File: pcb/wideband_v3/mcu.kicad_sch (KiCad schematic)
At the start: 44 parts, among them J1 Conn_01x14, J2 USB_C_Receptacle_USB2.0, J3 Tag connect, SW1 Key0, SW3 Key1, U1 RP2040, U2 W25Q128JVS, U8 AMS1117-3.3, Y1 12MHz

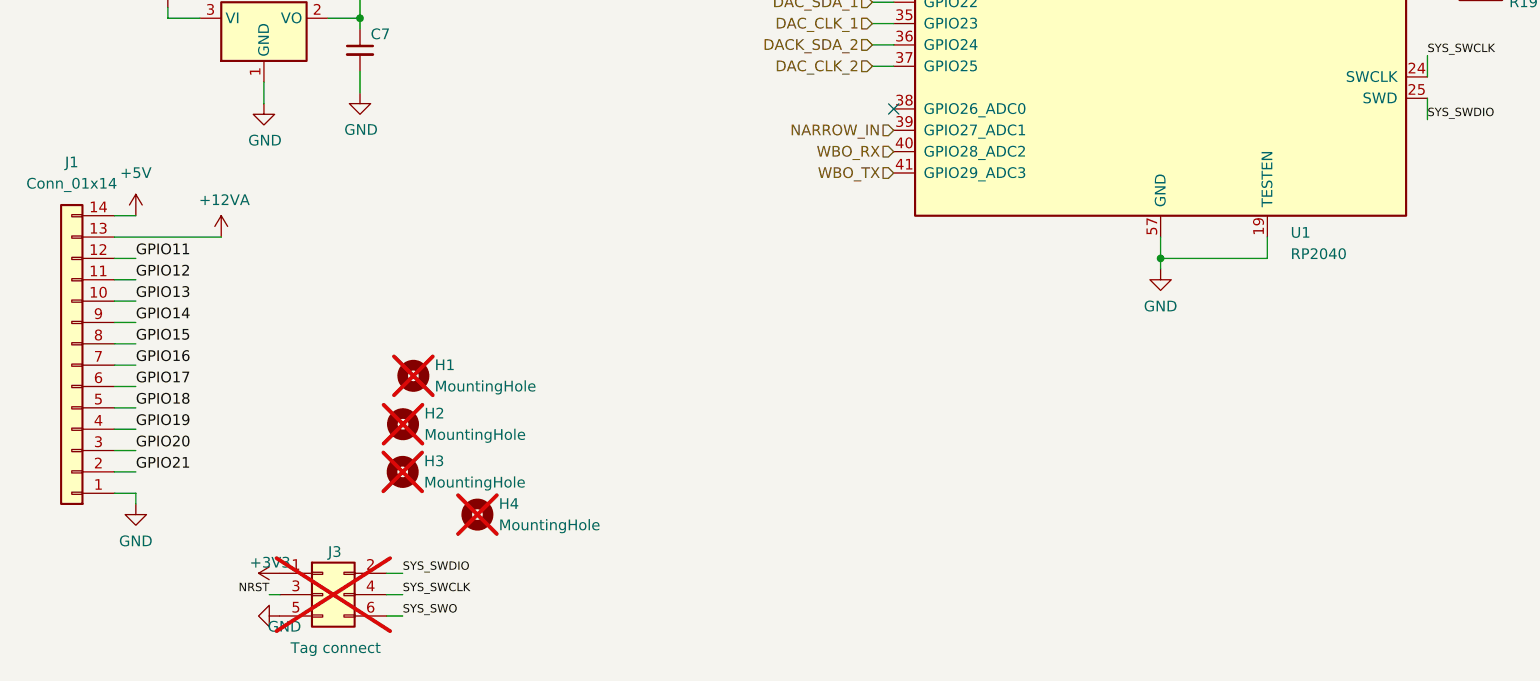
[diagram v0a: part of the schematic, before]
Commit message: reorganize rev3 diagram, add display code to carrier fw
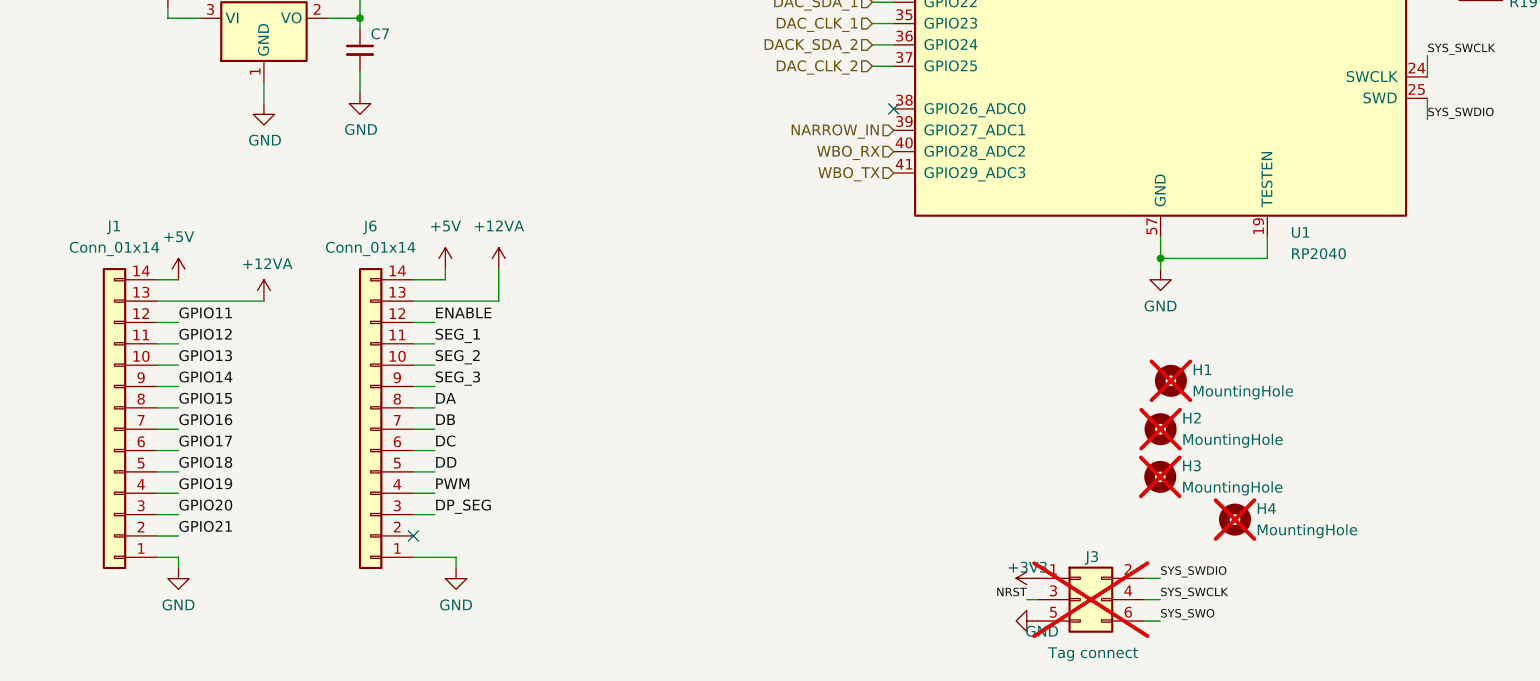
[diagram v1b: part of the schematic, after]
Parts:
- added J6: Conn_01x14, Connector_PinHeader_2.54mm:PinHeader_2x07_P2.54mm_Vertical, symbol Connector_Generic:Conn_01x14
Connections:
- net +12VA: now also J6.13 (Pin_13)
- net +5V: now also J6.14 (Pin_14)
- net GND: now also J6.1 (Pin_1)
- new net DA: J6.8 (Pin_8)
- new net DB: J6.7 (Pin_7)
- new net DC: J6.6 (Pin_6)
- new net DD: J6.5 (Pin_5)
- new net DP_SEG: J6.3 (Pin_3)
- new net ENABLE: J6.12 (Pin_12)
- new net PWM: J6.4 (Pin_4)
- new net SEG_1: J6.11 (Pin_11)
- new net SEG_2: J6.10 (Pin_10)
- new net SEG_3: J6.9 (Pin_9)
- no-connect marks 9 -> 10
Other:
- moved on the sheet: H1, H2, H3, H4, J1, J3
